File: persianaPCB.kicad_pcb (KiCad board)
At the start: 2 copper layers, 51 x 101 mm, 50 parts, among them J1 BORNERA-2, J2 Conn_01x05_Male, J3 BORNERA-3, J4 BORNERA-3, J5 BORNERA-2, J6 BORNERA-2, K1 SANYOU_SRD_Form_C, K2 SANYOU_SRD_Form_C, Q1 2N7002K, Q2 2N7002K, SW1 TACT-SWITCH 7 mm, U1 LM2596S-ADJ, U2 LM1117-3.3, U3 ESP-12F, U4 TLP621, U5 TLP621

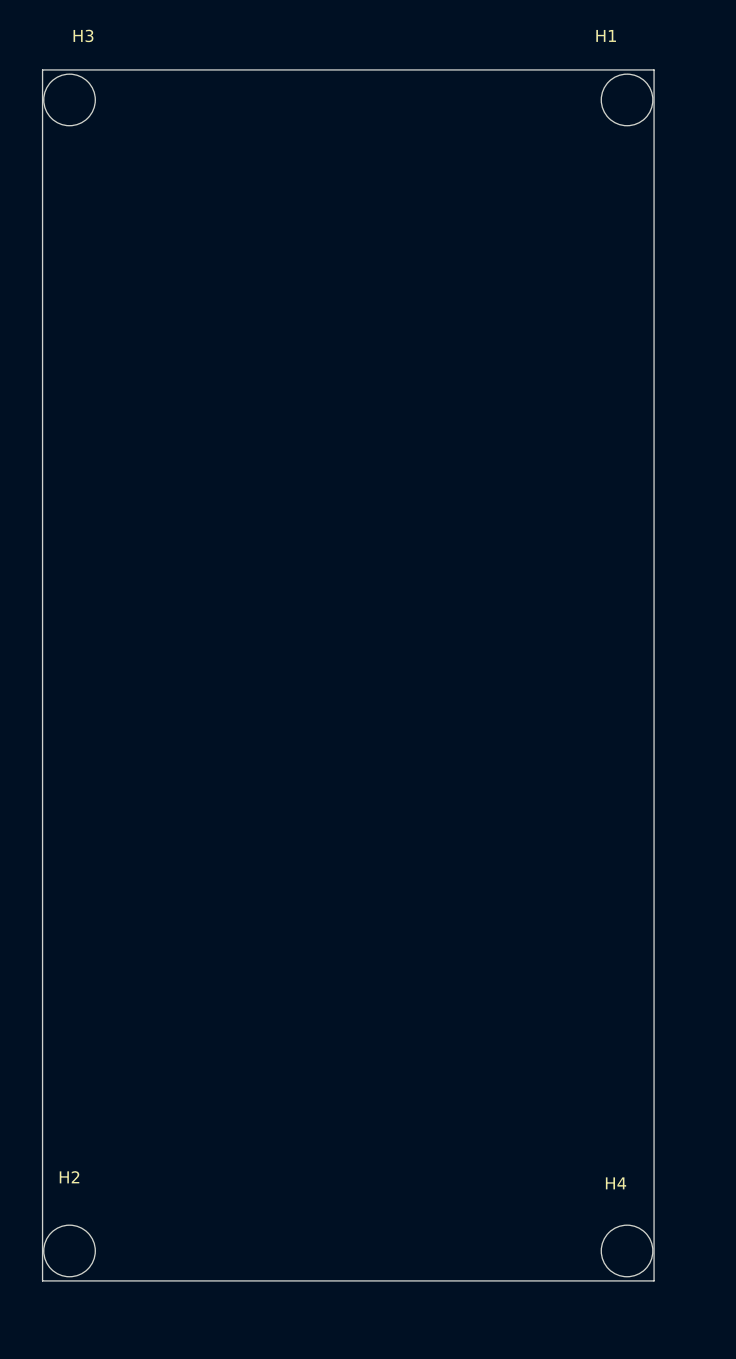
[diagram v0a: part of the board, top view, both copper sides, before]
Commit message: cambios en tamaño y agujeros de fijación
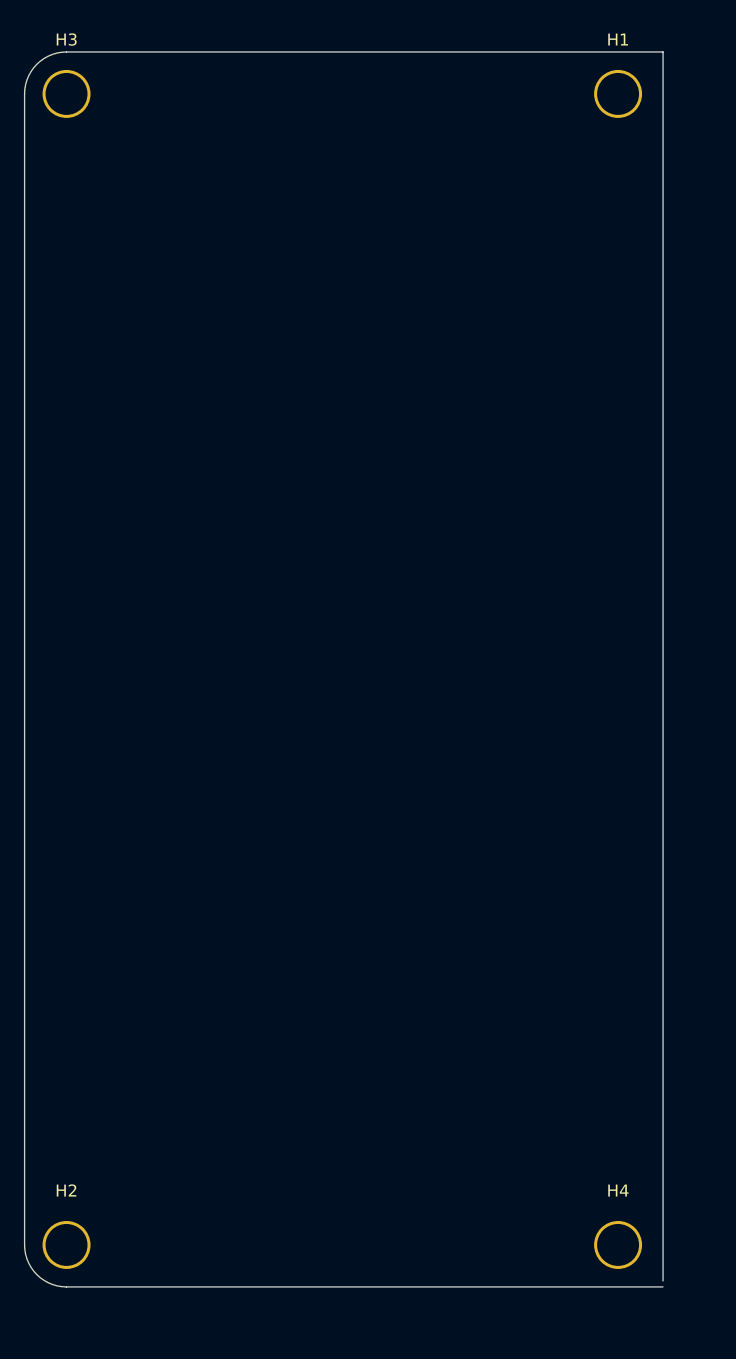
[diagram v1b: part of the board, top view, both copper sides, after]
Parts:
- H1, H2, H3, H4: value MountingHole -> 3.5; footprint MountingHole:MountingHole_4.3mm_M4 -> MountingHole:MountingHole_3.5mm_Pad
- moved H3 1.49 mm to (22.0, 22.0)
- moved H1 1.12 mm to (68.0, 22.0)
- moved H2 0.39 mm to (22.0, 118.0)
- moved H4 0.28 mm to (68.0, 118.0)
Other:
- board size 51 x 101 mm -> 53.2 x 103 mm

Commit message: avance en PCB y SCH
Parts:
- added D10: LED, LED_SMD:LED_0805_2012Metric_Pad1.15x1.40mm_HandSolder, F.Cu at (48.4, 43.4)
- added D7: LED, LED_SMD:LED_0805_2012Metric_Pad1.15x1.40mm_HandSolder, F.Cu at (61.4, 86.2)
- added D8: LED, LED_SMD:LED_0805_2012Metric_Pad1.15x1.40mm_HandSolder, F.Cu at (27.2, 86.2)
- added D9: LED, LED_SMD:LED_0805_2012Metric_Pad1.15x1.40mm_HandSolder, F.Cu at (63.6, 41.6)
- added R12: 1K, Resistor_SMD:R_0805_2012Metric_Pad1.20x1.40mm_HandSolder, F.Cu at (56.8, 86.2)
- added R13: 1K, Resistor_SMD:R_0805_2012Metric_Pad1.20x1.40mm_HandSolder, F.Cu at (31.6, 86.2)
- D1, D3, D4, D5, D6: footprint Diode_SMD:D_MELF -> Diode_SMD:D_SMA_Handsoldering
- H1, H2, H3, H4: value 3.5 -> 4mm; footprint MountingHole:MountingHole_3.5mm_Pad -> MountingHole:MountingHole_4mm_Pad
- J2: value Conn_01x05_Male -> Conn_01x06_Male; footprint Connector_PinHeader_2.54mm:PinHeader_1x05_P2.54mm_Vertical -> Connector_PinHeader_2.54mm:PinHeader_1x06_P2.54mm_Vertical
- Q1, Q2: footprint Package_TO_SOT_SMD:SOT-23 -> Package_TO_SOT_SMD:SOT-23_Handsoldering
- SW1: footprint Button_Switch_THT:SW_PUSH_6mm -> Button_Switch_THT:SW_Tactile_SPST_Angled_PTS645Vx39-2LFS
- moved J1 238.1 mm to (34.6, 30.0), turned to 180 degrees
- moved D6 212.5 mm to (37.6, 41.4), turned to 90 degrees
- moved R11 204.8 mm to (48.4, 39.2), turned to -90 degrees
- moved R10 204.7 mm to (42.4, 53.6), turned to 90 degrees
- moved J6 200.9 mm to (46.8, 30.0), turned to 180 degrees
- moved U5 200.0 mm to (44.7, 38.8), turned to -90 degrees
- moved D5 197.4 mm to (53.2, 41.2), turned to 90 degrees
- moved R9 193.5 mm to (64.6, 38.0), turned to -90 degrees
- moved C8 193.0 mm to (50.4, 49.8), turned to 90 degrees
- moved D1 188.2 mm to (23.2, 32.4), turned to 90 degrees
- moved R4 188.1 mm to (65.4, 49.6), turned to 180 degrees
- moved C10 186.9 mm to (48.0, 49.8), turned to 90 degrees
- moved R8 185.7 mm to (66.2, 44.8), turned to 90 degrees
- moved U4 183.6 mm to (59.8, 39.0), turned to -90 degrees
- moved C2 182.8 mm to (21.4, 52.0), turned to 90 degrees
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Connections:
- C2 pad 1: Net-(C2-Pad1) -> +VSW
- C3 pad 1: Net-(C2-Pad1) -> +VSW
- D1 pad 1: Net-(C2-Pad1) -> +VSW
- D5 pad 2: Net-(D5-Pad2) -> GND
- D6 pad 2: Net-(D6-Pad2) -> GND
- J1 pad 1: /fuente/VIN -> GND
- J1 pad 2: GND -> /fuente/VIN
- J4 pad 1: Net-(J4-Pad1) -> Net-(K2-Pad3)
- J4 pad 3: Net-(J4-Pad3) -> Net-(K2-Pad4)
- J5 pad 1: Net-(J5-Pad1) -> +VSW
- J5 pad 2: Net-(D5-Pad2) -> Net-(J5-Pad2)
- J6 pad 1: Net-(J6-Pad1) -> +VSW
- J6 pad 2: Net-(D6-Pad2) -> Net-(J6-Pad2)
- K1 pad 3: Net-(J3-Pad3) -> Net-(J3-Pad1)
- K1 pad 4: Net-(J3-Pad1) -> Net-(J3-Pad3)
- K2 pad 3: Net-(J4-Pad3) -> Net-(K2-Pad3)
- K2 pad 4: Net-(J4-Pad1) -> Net-(K2-Pad4)
- R11 pad 1: Net-(J6-Pad1) -> Net-(J6-Pad2)
- R9 pad 1: Net-(J5-Pad1) -> Net-(J5-Pad2)
- U1 pad 1: Net-(C2-Pad1) -> +VSW
- U4 pad 1: Net-(D5-Pad1) -> Net-(U4-Pad1)
- U4 pad 2: Net-(D5-Pad2) -> GND
- U5 pad 1: Net-(D6-Pad1) -> Net-(U5-Pad1)
- U5 pad 2: Net-(D6-Pad2) -> GND
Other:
- board size 53.2 x 103 mm -> 53 x 103 mm

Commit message: avance en PCB y SCH
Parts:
- J2: value Conn_01x06_Male -> PINM-6
- U2: footprint Package_TO_SOT_SMD:TO-252-3_TabPin2 -> Package_TO_SOT_SMD:SOT-223-3_TabPin2
- moved R7 17.3 mm to (39.4, 84.6), turned to 90 degrees
- moved R6 17.0 mm to (51.6, 84.6), turned to -90 degrees
- moved D7 17.0 mm to (69.0, 101.4), turned to -90 degrees
- moved D8 16.3 mm to (21.4, 101.4), turned to -90 degrees
- moved R12 13.2 mm to (69.0, 91.2), turned to -90 degrees
- moved R3 13.0 mm to (48.8, 76.6)
- moved Q2 12.6 mm to (33.8, 84.6), turned to 180 degrees
- moved Q1 12.5 mm to (56.6, 84.6), turned to 0 degrees
- moved D4 12.2 mm to (24.6, 84.6), turned to 0 degrees
- moved D3 11.9 mm to (65.6, 84.6), turned to 180 degrees
- moved R13 11.5 mm to (21.4, 91.6), turned to -90 degrees
- moved R8 11.0 mm to (56.4, 49.8), turned to 180 degrees
- moved D6 7.89 mm to (45.4, 42.6), turned to -90 degrees
- moved D5 6.16 mm to (59.2, 42.6)
- moved R5 5.44 mm to (55.0, 76.4)
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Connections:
- D7 pad 1: Net-(D3-Pad2) -> Net-(R12-Pad2)
- D7 pad 2: Net-(D7-Pad2) -> +5V
- D8 pad 1: Net-(D4-Pad2) -> Net-(R13-Pad2)
- D8 pad 2: Net-(D8-Pad2) -> +5V
- J2 pad 1: Net-(J2-Pad1) -> GND
- J2 pad 3: Net-(J2-Pad3) -> unconnected-(J2-Pad3)
- J2 pad 5: GND -> Net-(J2-Pad5)
- J2 pad 6: unconnected-(J2-Pad6) -> Net-(J2-Pad6)
- J3 pad 1: Net-(J3-Pad1) -> Net-(K1-Pad4)
- J3 pad 2: Net-(J3-Pad2) -> Net-(K1-Pad3)
- J3 pad 3: Net-(J3-Pad3) -> Net-(K1-Pad1)
- J4 pad 1: Net-(K2-Pad3) -> Net-(K2-Pad1)
- J4 pad 2: Net-(J4-Pad2) -> Net-(K2-Pad4)
- J4 pad 3: Net-(K2-Pad4) -> Net-(K2-Pad3)
- J5 pad 1: +VSW -> Net-(J5-Pad1)
- J5 pad 2: Net-(J5-Pad2) -> +VSW
- J6 pad 1: +VSW -> Net-(J6-Pad1)
- J6 pad 2: Net-(J6-Pad2) -> +VSW
- K1 pad 1: Net-(J3-Pad2) -> Net-(K1-Pad1)
- K1 pad 3: Net-(J3-Pad1) -> Net-(K1-Pad3)
- K1 pad 4: Net-(J3-Pad3) -> Net-(K1-Pad4)
- K2 pad 1: Net-(J4-Pad2) -> Net-(K2-Pad1)
- K2 pad 2: Net-(D4-Pad2) -> +5V
- K2 pad 5: +5V -> Net-(D4-Pad2)
- R10 pad 2: /core/GPIO5 -> /core/GPIO14
- R11 pad 1: Net-(J6-Pad2) -> Net-(J6-Pad1)
- R12 pad 1: Net-(D7-Pad2) -> Net-(D3-Pad2)
- R12 pad 2: +5V -> Net-(R12-Pad2)
- R13 pad 1: Net-(D8-Pad2) -> Net-(D4-Pad2)
- R13 pad 2: +5V -> Net-(R13-Pad2)
- R3 pad 1: Net-(J2-Pad1) -> Net-(J2-Pad6)
- R4 pad 1: Net-(J2-Pad3) -> Net-(J2-Pad2)
- R8 pad 2: /core/GPIO4 -> /core/GPIO16
- R9 pad 1: Net-(J5-Pad2) -> Net-(J5-Pad1)
- U3 pad 1: Net-(J2-Pad3) -> Net-(J2-Pad2)
- U3 pad 18: Net-(J2-Pad1) -> Net-(J2-Pad6)
- U3 pad 19: /core/GPIO4 -> unconnected-(U3-Pad19)
- U3 pad 20: /core/GPIO5 -> unconnected-(U3-Pad20)
- U3 pad 22: Net-(J2-Pad2) -> Net-(J2-Pad5)
- U3 pad 4: Net-(R5-Pad2) -> /core/GPIO16
- U3 pad 5: unconnected-(U3-Pad5) -> /core/GPIO14
- U4 pad 4: /core/GPIO4 -> /core/GPIO16
- U5 pad 4: /core/GPIO5 -> /core/GPIO14
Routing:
- net +5V: track 0.00 -> 84.2 mm
- net +VSW: track 0.00 -> 29.0 mm
- net Net-(K2-Pad4): track 0.00 -> 22.2 mm
- net Net-(K1-Pad3): track 0.00 -> 22.2 mm
- net /core/GPIO14: track 0.00 -> 19.9 mm
- net Net-(K2-Pad1): track 0.00 -> 19.8 mm
- net Net-(K1-Pad1): track 0.00 -> 19.8 mm
- net Net-(D3-Pad2): track 0.00 -> 17.8 mm
- net Net-(D4-Pad2): track 0.00 -> 17.7 mm
- net Net-(C1-Pad1): track 0.00 -> 14.3 mm
- net Net-(D2-Pad1): track 0.00 -> 13.5 mm
- net Net-(D5-Pad1): track 0.00 -> 10.7 mm
- net Net-(D9-Pad1): track 0.00 -> 10.2 mm
- net Net-(D10-Pad1): track 0.00 -> 10.1 mm
- net Net-(D10-Pad2): track 0.00 -> 9.58 mm
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
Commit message: avances finales
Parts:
- removed C9: 4,7uF, Capacitor_SMD:C_0805_2012Metric_Pad1.18x1.45mm_HandSolder
- added R14: 10K, Resistor_SMD:R_0805_2012Metric_Pad1.20x1.40mm_HandSolder, F.Cu at (52.0, 72.8)
- added R15: 10K, Resistor_SMD:R_0805_2012Metric_Pad1.20x1.40mm_HandSolder, F.Cu at (49.6, 72.8)
- moved SW1 45.2 mm to (68.1, 29.9)
- moved R5 27.4 mm to (56.0, 49.0), turned to 90 degrees
- moved Q1 7.20 mm to (49.4, 84.6)
- moved R6 7.20 mm to (44.4, 84.6)
- moved D3 7.20 mm to (58.4, 84.6)
- moved R3 6.60 mm to (54.2, 72.8), turned to -90 degrees
- moved R8 3.49 mm to (53.0, 49.0), turned to 90 degrees
- moved TP1 2.60 mm to (38.0, 74.8)
- moved TP2 1.61 mm to (38.0, 78.6)
- moved R7 1.40 mm to (39.4, 83.2)
- moved Q2 1.20 mm to (33.8, 83.4)
- moved R4 0.89 mm to (60.8, 49.0), turned to -90 degrees
- moved D5 0.80 mm to (59.2, 41.8)
- moved D6 0.80 mm to (45.4, 41.8)
- moved R11 0.80 mm to (48.4, 38.4)
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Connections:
- Q1 pad 1: /core/GPIO12 -> /core/GPIO5
- Q2 pad 1: /core/GPIO13 -> /core/GPIO4
- R10 pad 2: /core/GPIO14 -> /core/GPIO13
- R5 pad 2: Net-(R5-Pad2) -> Net-(U3-Pad4)
- R6 pad 1: /core/GPIO12 -> /core/GPIO5
- R7 pad 1: /core/GPIO13 -> /core/GPIO4
- R8 pad 2: /core/GPIO16 -> /core/GPIO14
- SW1 pad 1: Net-(R5-Pad2) -> GND
- SW1 pad 2: GND -> Net-(U3-Pad4)
- U3 pad 16: unconnected-(U3-Pad16) -> Net-(U3-Pad16)
- U3 pad 17: unconnected-(U3-Pad17) -> Net-(U3-Pad17)
- U3 pad 19: unconnected-(U3-Pad19) -> /core/GPIO4
- U3 pad 20: unconnected-(U3-Pad20) -> /core/GPIO5
- U3 pad 4: /core/GPIO16 -> Net-(U3-Pad4)
- U3 pad 6: /core/GPIO12 -> unconnected-(U3-Pad6)
- U4 pad 4: /core/GPIO16 -> /core/GPIO14
- U5 pad 4: /core/GPIO14 -> /core/GPIO13
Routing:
- net GND: track 0.00 -> 293.6 mm, vias 0 -> 7
- net +5V: track 84.2 -> 171.1 mm, vias 0 -> 2
- net +3V3: track 0.00 -> 85.9 mm
- net +VSW: track 29.0 -> 78.9 mm
- net Net-(J2-Pad2): track 0.00 -> 37.0 mm, vias 0 -> 1
- net /core/GPIO5: track 0.00 -> 33.4 mm, vias 0 -> 2
- net /core/GPIO4: track 0.00 -> 32.4 mm
- net Net-(U3-Pad4): track 0.00 -> 31.4 mm, vias 0 -> 2
- net Net-(J2-Pad5): track 0.00 -> 21.9 mm
- net /core/GPIO13: track 0.00 -> 21.5 mm, vias 0 -> 1
- net Net-(J2-Pad6): track 0.00 -> 17.4 mm
- net Net-(J2-Pad4): track 0.00 -> 16.8 mm
- net /core/GPIO16: track 7.92 -> 0.00 mm
- net /core/GPIO14: track 19.9 -> 13.0 mm, vias 0 -> 1
- net Net-(U3-Pad16): track 0.00 -> 2.81 mm
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- added copper zone on B.Cu, net GND
- added copper zone on F.Cu, net GND

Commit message: avance final!
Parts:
- moved C8 8.63 mm to (44.2, 55.0), turned to -90 degrees
- turned D5 to -90 degrees
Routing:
- net GND: track 293.6 -> 289.3 mm, vias 7 -> 30
- net +3V3: track 85.9 -> 89.8 mm
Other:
- board text added: "8V - 24V"
- board text added: "COM"
- board text added: "GND"
- board text added: "IN1"
- board text added: "IN2"
- board text added: "IO-WIFI V1.0"
- board text added: "NA"
- board text added: "NC"
- board text added: "OUT1"
- board text added: "OUT2"
- board text added: "VIN"
- board text added: "www.dsi.fceia.unr.edu.ar"

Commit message: cambios menores
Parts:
- turned D10 to 90 degrees
- turned D9 to 90 degrees
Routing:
- net Net-(D5-Pad1): track 9.80 -> 5.42 mm
- net Net-(D10-Pad2): track 9.58 -> 5.22 mm
- net Net-(D9-Pad1): track 10.2 -> 10.9 mm
- net Net-(D10-Pad1): track 10.1 -> 10.7 mm
- net Net-(J2-Pad5): track 21.9 -> 21.3 mm
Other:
- board text added: "8.5V - 36V"
- board text removed: "8V - 24V"

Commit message: cambios menores en valores de componentes
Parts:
- R1: value 1K -> 3K3
- R2: value 3,1K -> 10K
